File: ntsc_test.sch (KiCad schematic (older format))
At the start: 28 parts, among them P1 ICSP, SW1 power, U1 PIC12F1572

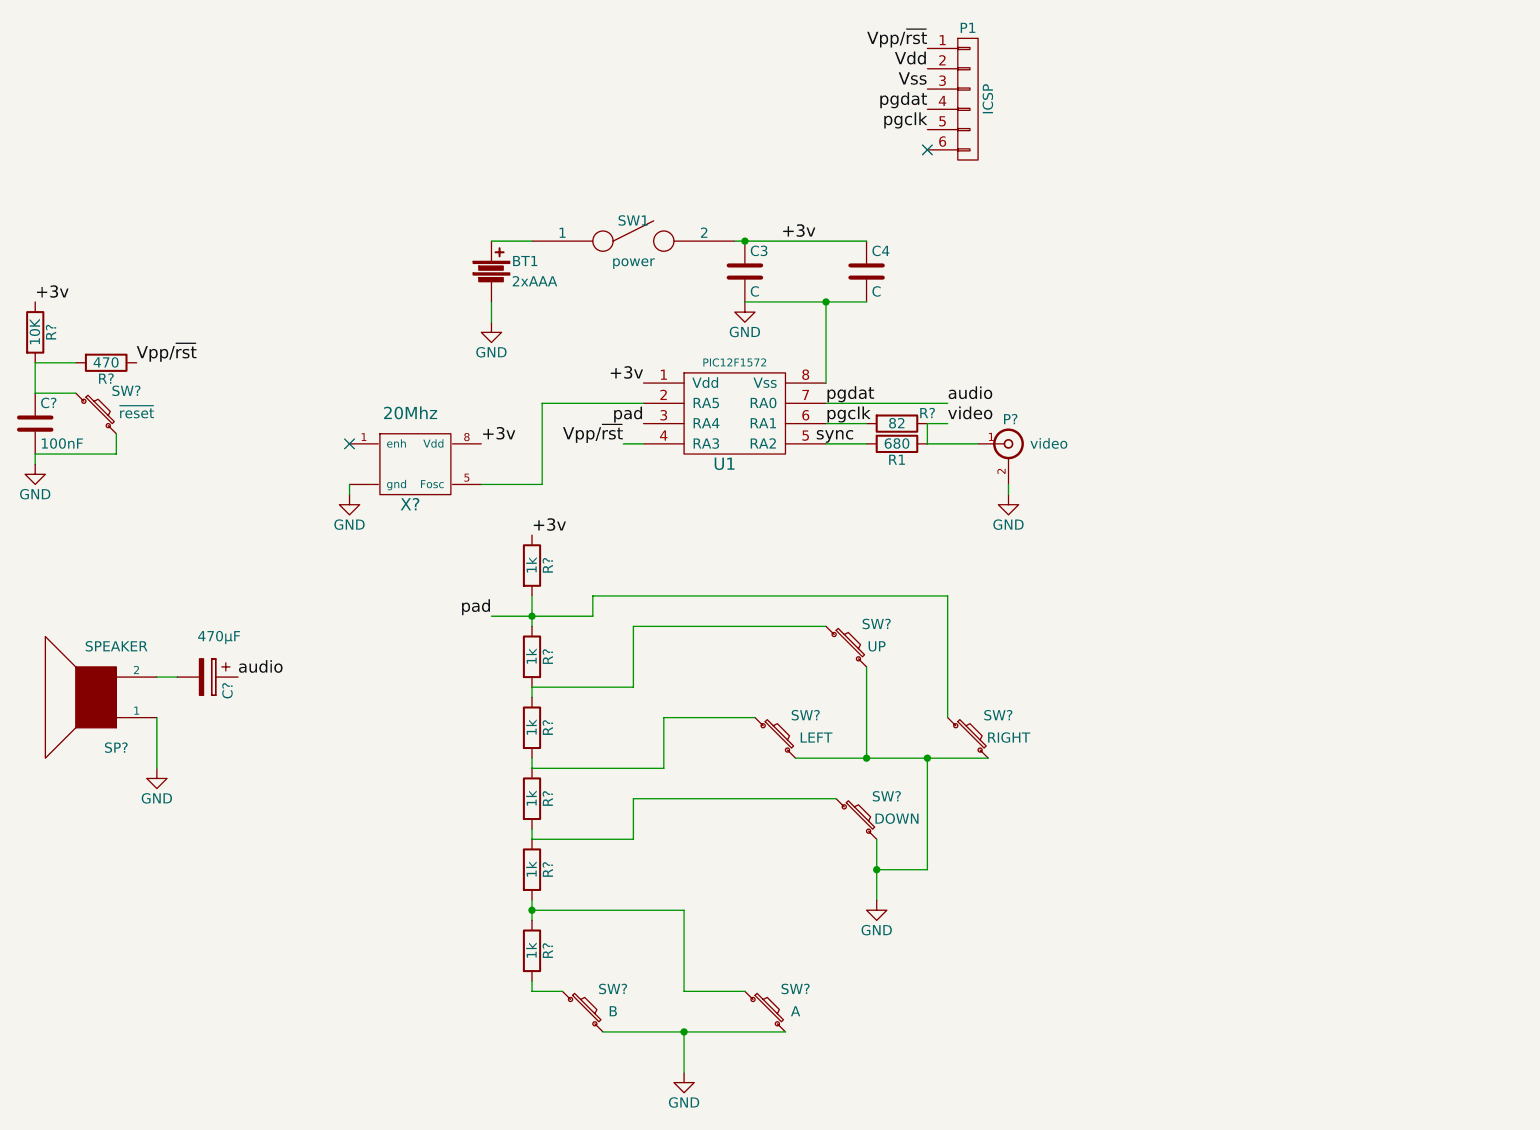
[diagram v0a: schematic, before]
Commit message: driver work
completed read_pad
modified isr
added print_terim and test code
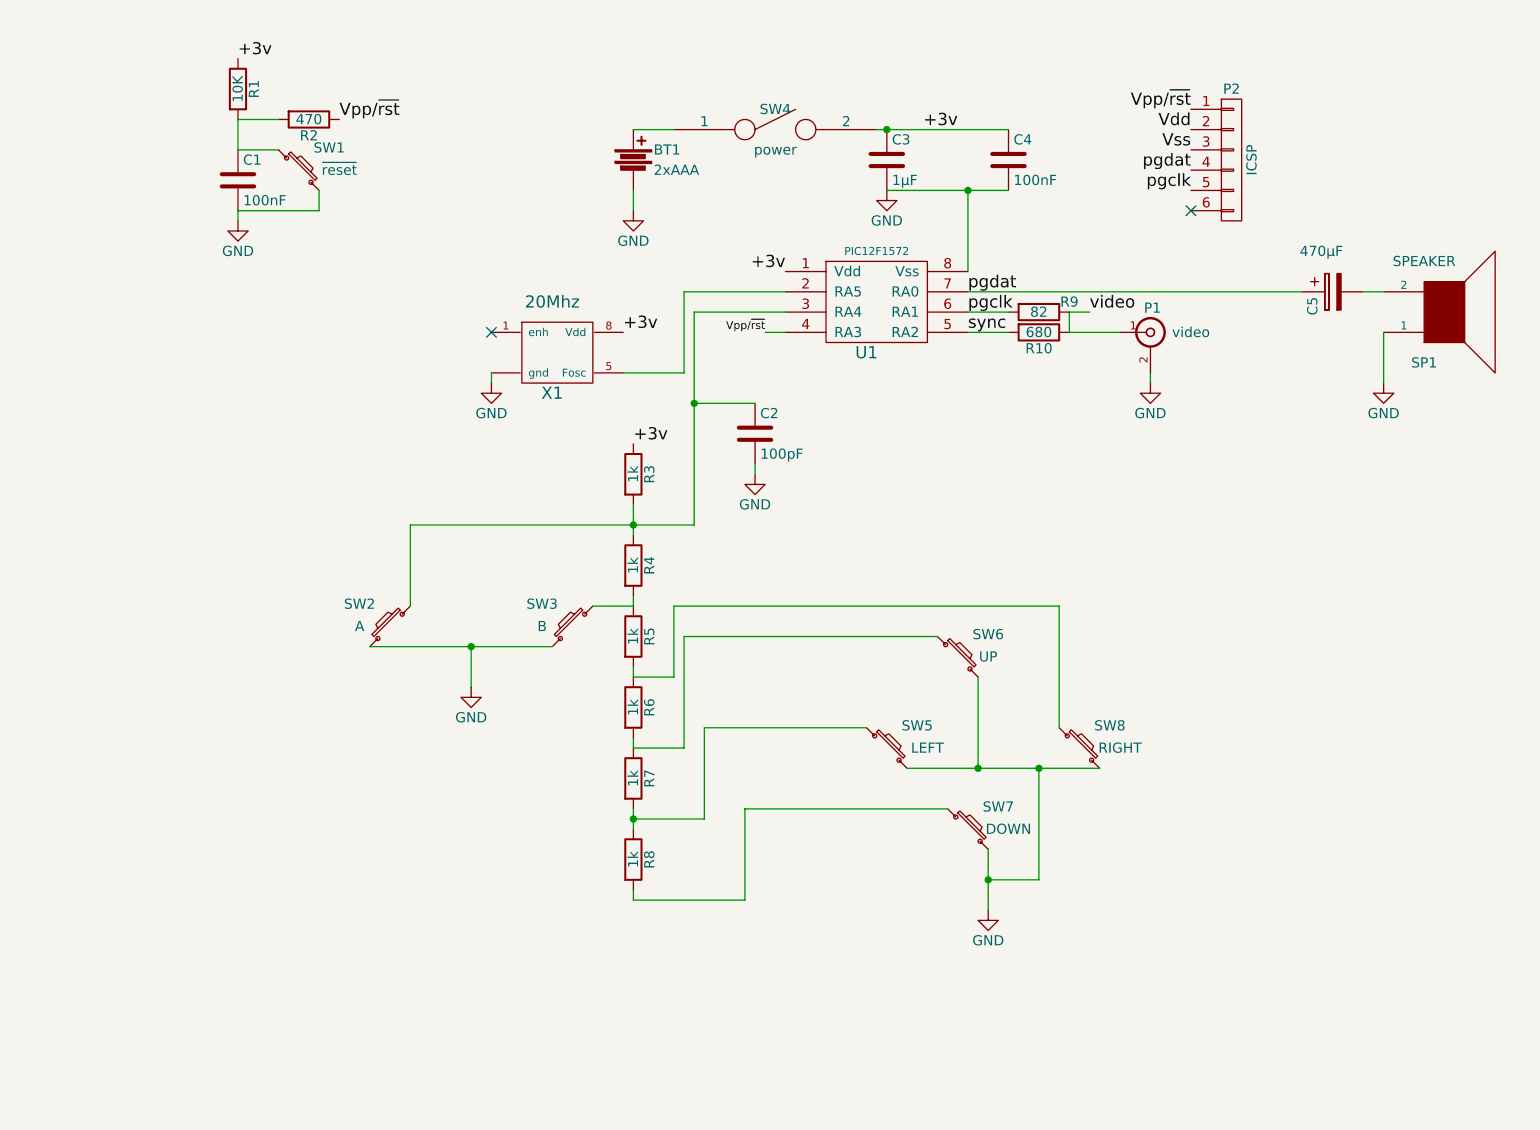
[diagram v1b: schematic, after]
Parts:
- added C2: 100pF, symbol C
- C3: value C -> 1µF
- C4: value C -> 100nF
- gave numbers to parts that had none: 21
- renumbered P1 to P2, R1 to R10, SW1 to SW4
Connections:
- net GND: now also C2.2
- net sync: now also R10.2, U1.5 (RA2)
- net at R4.2, R5.1: now also SW3.1; no longer SW6.1
- net at R5.2, R6.1: now also SW8.1; no longer SW5.1
- net at R6.2, R7.1: now also SW6.1; no longer SW7.1
- net at R7.2, R8.1: now also SW5.1; no longer SW2.1
- net at R8.2: now also SW7.1; no longer SW3.1
- net audio renamed pgdat
- net pad: no longer names the net of R3.2, R4.1, U1.3 (RA4)
- net pad: now also SW2.1, C2.1; no longer SW8.1
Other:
- moved on the sheet: BT1, C1, C3, C4, C5, P1, P2, R1, R10, R2, R3, R4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

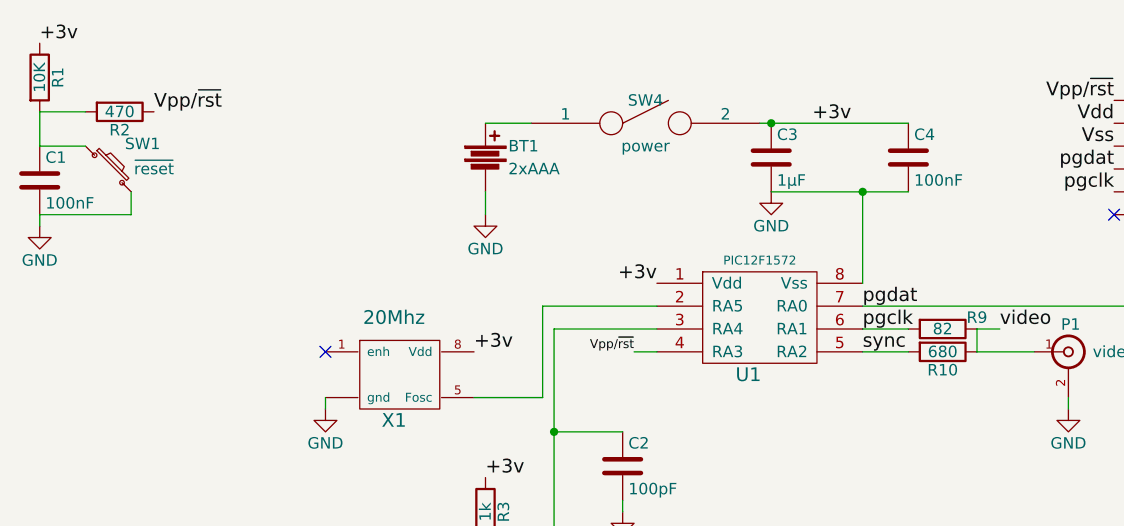
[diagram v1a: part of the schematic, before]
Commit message: added div10
modification to schematic
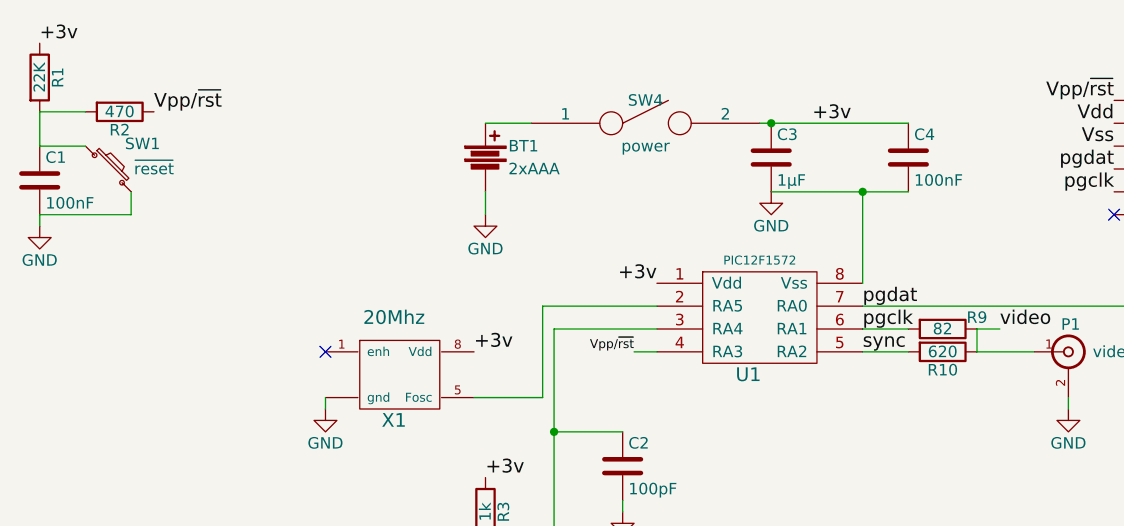
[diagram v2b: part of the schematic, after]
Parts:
- R1: value 10K -> 22K
- R10: value 680 -> 620
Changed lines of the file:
@@
 P 7350 3200
 F 0 "R10" V 7430 3200 50  0000 C CNN
-F 1 "680" V 7350 3200 50  0000 C CNN
+F 1 "620" V 7350 3200 50  0000 C CNN
 F 2 "" V 7280 3200 50  0000 C CNN
 F 3 "" H 7350 3200 50  0000 C CNN
@@
 P 3400 2000
 F 0 "R1" V 3480 2000 50  0000 C CNN
-F 1 "10K" V 3400 2000 50  0000 C CNN
+F 1 "22K" V 3400 2000 50  0000 C CNN
 F 2 "" V 3330 2000 50  0000 C CNN
 F 3 "" H 3400 2000 50  0000 C CNN

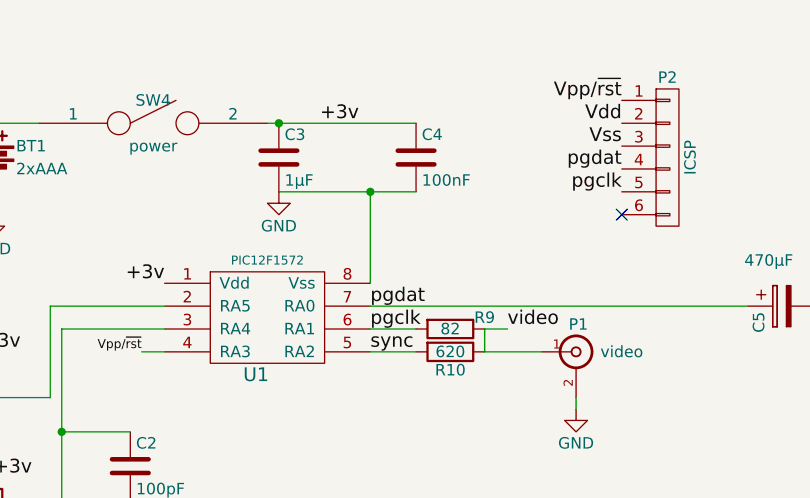
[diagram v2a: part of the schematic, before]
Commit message: added query_row
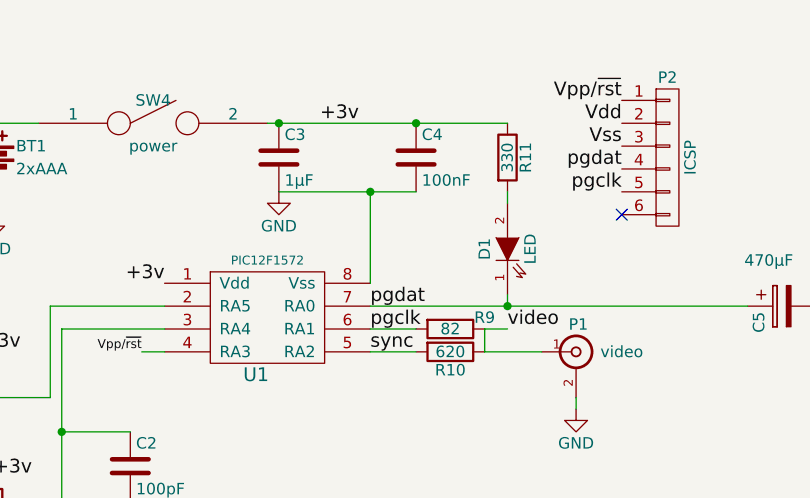
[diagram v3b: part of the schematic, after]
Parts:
- added D1: LED, symbol LED
- added R11: 330, symbol R
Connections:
- net +3v: now also R11.1
- net pgdat: now also D1.1 (K)
- new net: D1.2 (A), R11.2
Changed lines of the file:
@@
 	7200 2500 6600 2500
 Wire Wire Line
-	6550 2200 7200 2200
+	6550 2200 7600 2200
 Connection ~ 6600 2200
 Connection ~ 7000 2500
@@
 	5950 3550 5650 3550
 Connection ~ 5650 3550
+$Comp
+L LED D1
+U 1 1 584B6425
+P 7600 2750
+F 0 "D1" H 7600 2850 50  0000 C CNN
+F 1 "LED" H 7600 2650 50  0000 C CNN
+F 2 "" H 7600 2750 50  0000 C CNN
+F 3 "" H 7600 2750 50  0000 C CNN
+	1    7600 2750
+	0    -1   -1   0
+$EndComp
+$Comp
+L R R11
+U 1 1 584B656C
+P 7600 2350
+F 0 "R11" V 7680 2350 50  0000 C CNN
+F 1 "330" V 7600 2350 50  0000 C CNN
+F 2 "" V 7530 2350 50  0000 C CNN
+F 3 "" H 7600 2350 50  0000 C CNN
+	1    7600 2350
+	1    0    0    -1
+$EndComp
+Wire Wire Line
+	7600 2500 7600 2550
+Wire Wire Line
+	7600 2950 7600 3000
+Connection ~ 7600 3000
+Connection ~ 7200 2200
 $EndSCHEMATC

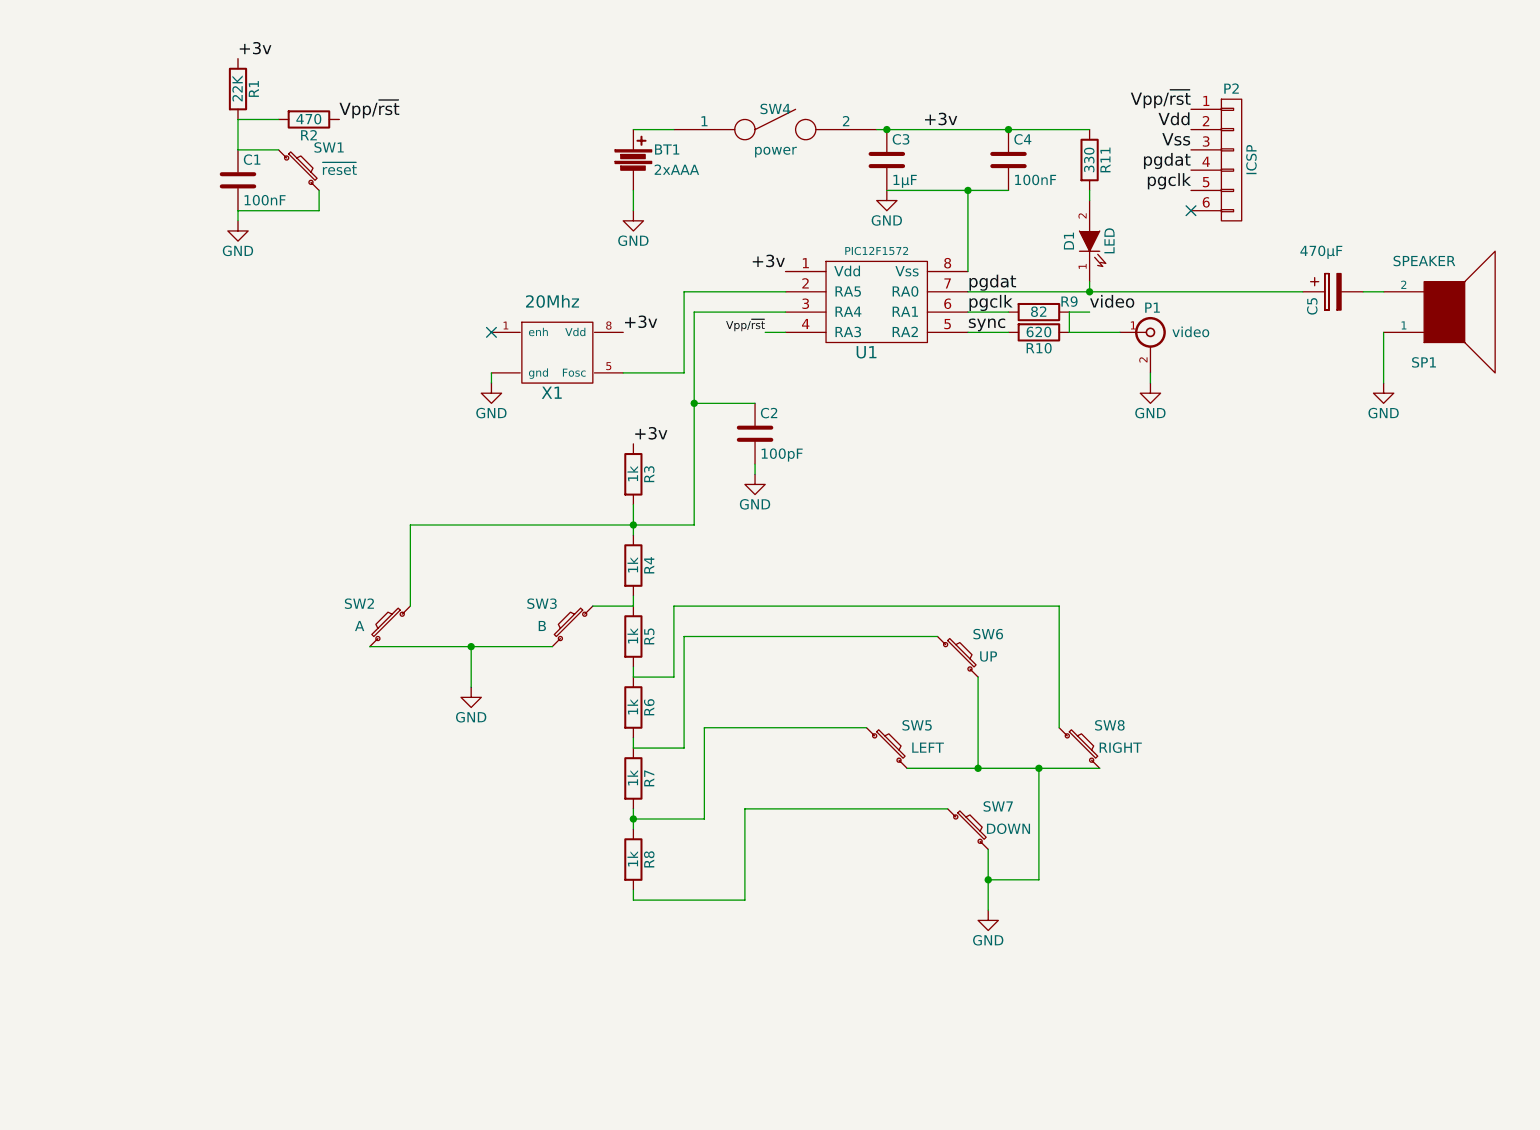
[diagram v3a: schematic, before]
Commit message: modified schematic
added audio support
added tone
added koromeiniki tune
added wait_start
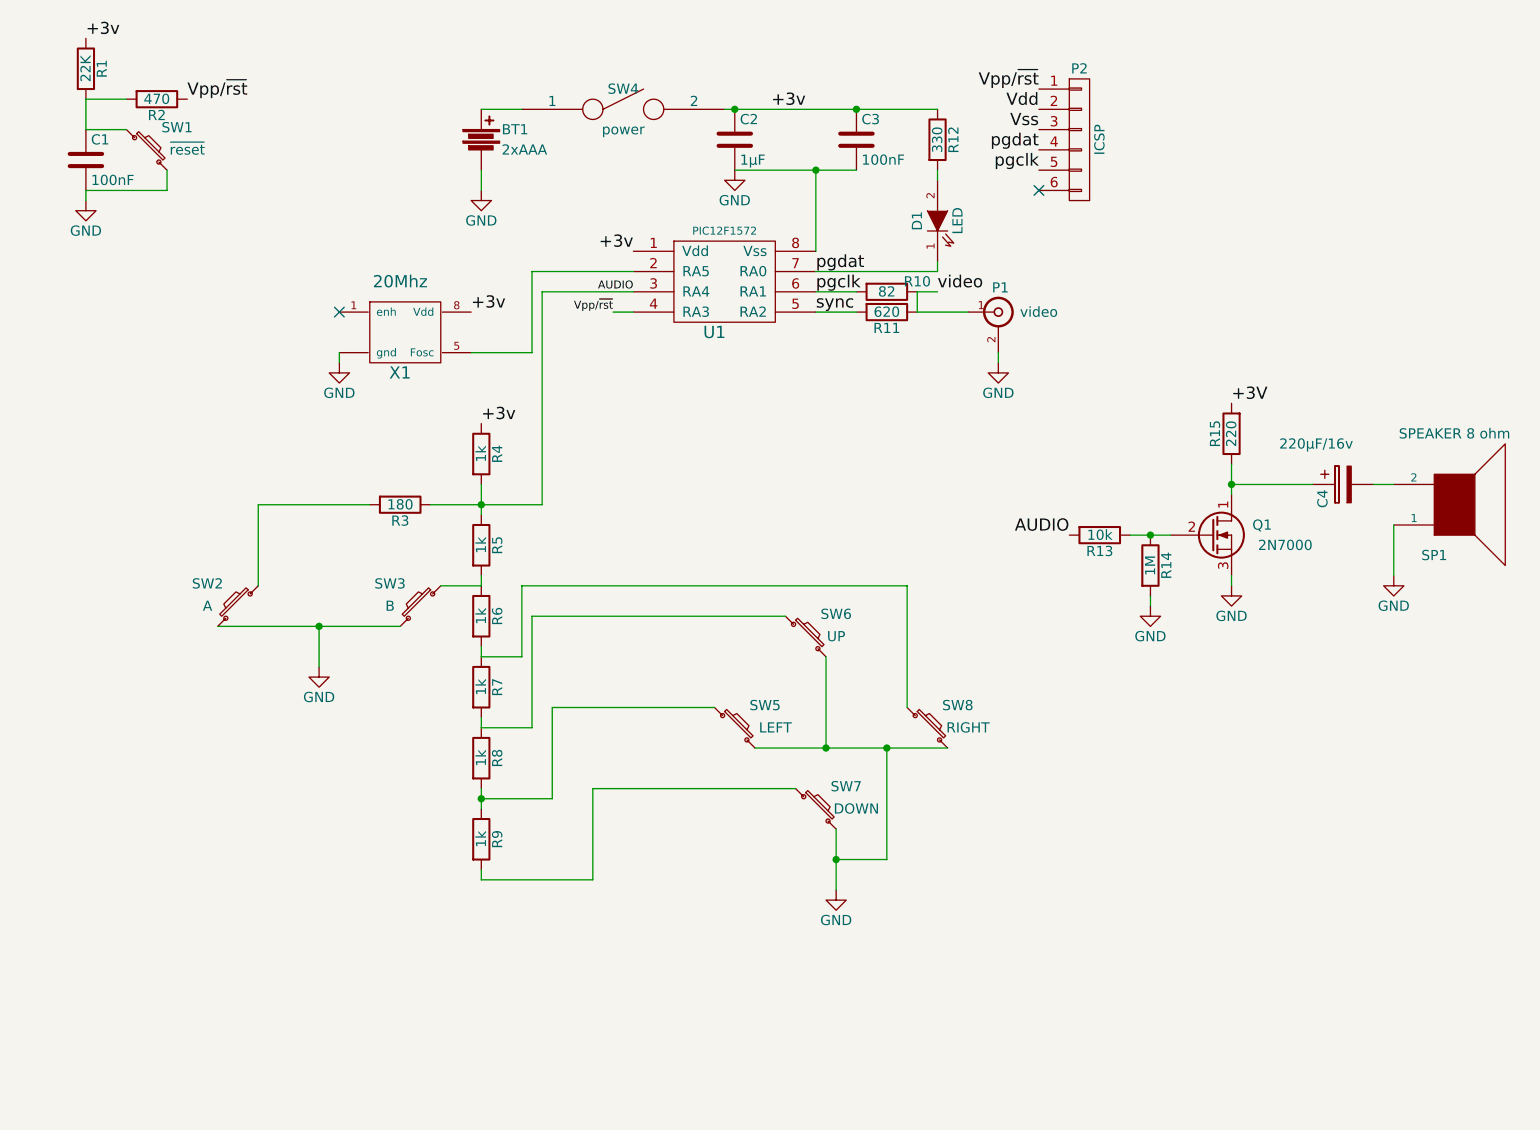
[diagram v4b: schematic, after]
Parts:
- removed C2: 100pF, symbol C
- added Q1: 2N7000, symbol Q_NMOS_DGS
- added R13: 10k, symbol R
- added R14: 1M, symbol R
- added R15: 220, symbol R
- added R3: 180, symbol R
- C4: renamed from C5; value 470µF -> 220µF/16v
- SP1: value SPEAKER -> SPEAKER 8 ohm
- renumbered C3 to C2, C4 to C3, R9 to R10, R10 to R11, R11 to R12, R3 to R4, R4 to R5, R5 to R6, R6 to R7, R7 to R8, R8 to R9
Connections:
- net GND: now also Q1.3 (S), R14.2
- net pgdat: no longer C4.1
- net AUDIO: now reaches R4.2, R5.1, U1.3 (RA4)
- net AUDIO: now also R13.2, R3.1; no longer SW2.1
- new net: R3.2, SW2.1
- new net: C4.1, Q1.1 (D), R15.1
- new net: Q1.2 (G), R13.1, R14.1
- new net +3V: R15.2
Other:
- moved on the sheet: BT1, C1, C2, C3, C4, D1, P1, P2, R1, R10, R11, R12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
